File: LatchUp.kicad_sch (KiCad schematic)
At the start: 27 parts, among them Q10 IRF7406, Q11 BSL307SP, Q9 BSS138, U25 INA138NA_3K, U26 AD589JRZ, U27 LT1636CMS8_PBF

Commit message: Update the manufacturer part number for some of components to be compatible with avaiable parts in the JLC parts database
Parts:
- C101: JLCPCB Part # (none) -> C141069; Manufacturer_Part_Number (none) -> C0603C102K5RACAUTO
- C90, C91: JLCPCB Part # C1591 -> C129621; Manufacturer_Part_Number CL10B104KB8NNNC -> C0603C104K5RACAUTO
- C92: JLCPCB Part # C307479 -> C342956; Manufacturer_Part_Number CL10B105KA8NFNC -> CGA3E1X7R1V105KT000N
- D18: Manufacturer_Part_Number BZY55C2V7 RBG -> BZY55B2V7 RBG
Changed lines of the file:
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@@
       (effects (font (size 1.27 1.27)) hide)
     )
-    (property "JLCPCB Part #" "" (id 4) (at 88.9 91.44 0)
-      (effects (font (size 1.27 1.27)) hide)
-    )
-    (property "Manufacturer_Part_Number" "" (id 5) (at 88.9 91.44 0)
+    (property "JLCPCB Part #" "C141069" (id 4) (at 88.9 91.44 0)
+      (effects (font (size 1.27 1.27)) hide)
+    )
+    (property "Manufacturer_Part_Number" "C0603C102K5RACAUTO" (id 5) (at 88.9 91.44 0)
       (effects (font (size 1.27 1.27)) hide)
     )
@@
       (effects (font (size 1.27 1.27)) hide)
     )
-    (property "JLCPCB Part #" "C1591" (id 4) (at 30.48 81.28 0)
-      (effects (font (size 1.27 1.27)) hide)
-    )
-    (property "Manufacturer_Part_Number" "CL10B104KB8NNNC " (id 5) (at 30.48 81.28 0)
+    (property "JLCPCB Part #" "C129621" (id 4) (at 30.48 81.28 0)
+      (effects (font (size 1.27 1.27)) hide)
+    )
+    (property "Manufacturer_Part_Number" "C0603C104K5RACAUTO" (id 5) (at 30.48 81.28 0)
       (effects (font (size 1.27 1.27)) hide)
     )
@@
       (effects (font (size 1.27 1.27)) hide)
     )
-    (property "Manufacturer_Part_Number" "BZY55C2V7 RBG" (id 4) (at 180.34 100.33 90)
+    (property "Manufacturer_Part_Number" "BZY55B2V7 RBG " (id 4) (at 180.34 100.33 90)
       (effects (font (size 1.27 1.27)) hide)
     )
@@
       (effects (font (size 1.27 1.27)) hide)
     )
-    (property "JLCPCB Part #" "C1591" (id 4) (at 80.01 97.79 0)
-      (effects (font (size 1.27 1.27)) hide)
-    )
-    (property "Manufacturer_Part_Number" "CL10B104KB8NNNC " (id 5) (at 80.01 97.79 0)
+    (property "JLCPCB Part #" "C129621" (id 4) (at 80.01 97.79 0)
+      (effects (font (size 1.27 1.27)) hide)
+    )
+    (property "Manufacturer_Part_Number" "C0603C104K5RACAUTO" (id 5) (at 80.01 97.79 0)
       (effects (font (size 1.27 1.27)) hide)
     )
@@
       (effects (font (size 1.27 1.27)) hide)
     )
-    (property "JLCPCB Part #" "C307479" (id 4) (at 195.58 91.44 0)
-      (effects (font (size 1.27 1.27)) hide)
-    )
-    (property "Manufacturer_Part_Number" "CL10B105KA8NFNC " (id 5) (at 195.58 91.44 0)
-      (effects (font (size 1.27 1.27)) hide)
-    )
+    (property "JLCPCB Part #" "C342956" (id 4) (at 195.58 91.44 0)
+      (effects (font (size 1.27 1.27)) hide)
+    )
+    (property "Manufacturer_Part_Number" "CGA3E1X7R1V105KT000N" (id 5) (at 195.58 91.44 0)
+      (effects (font (size 1.27 1.27)) hide)
+    )

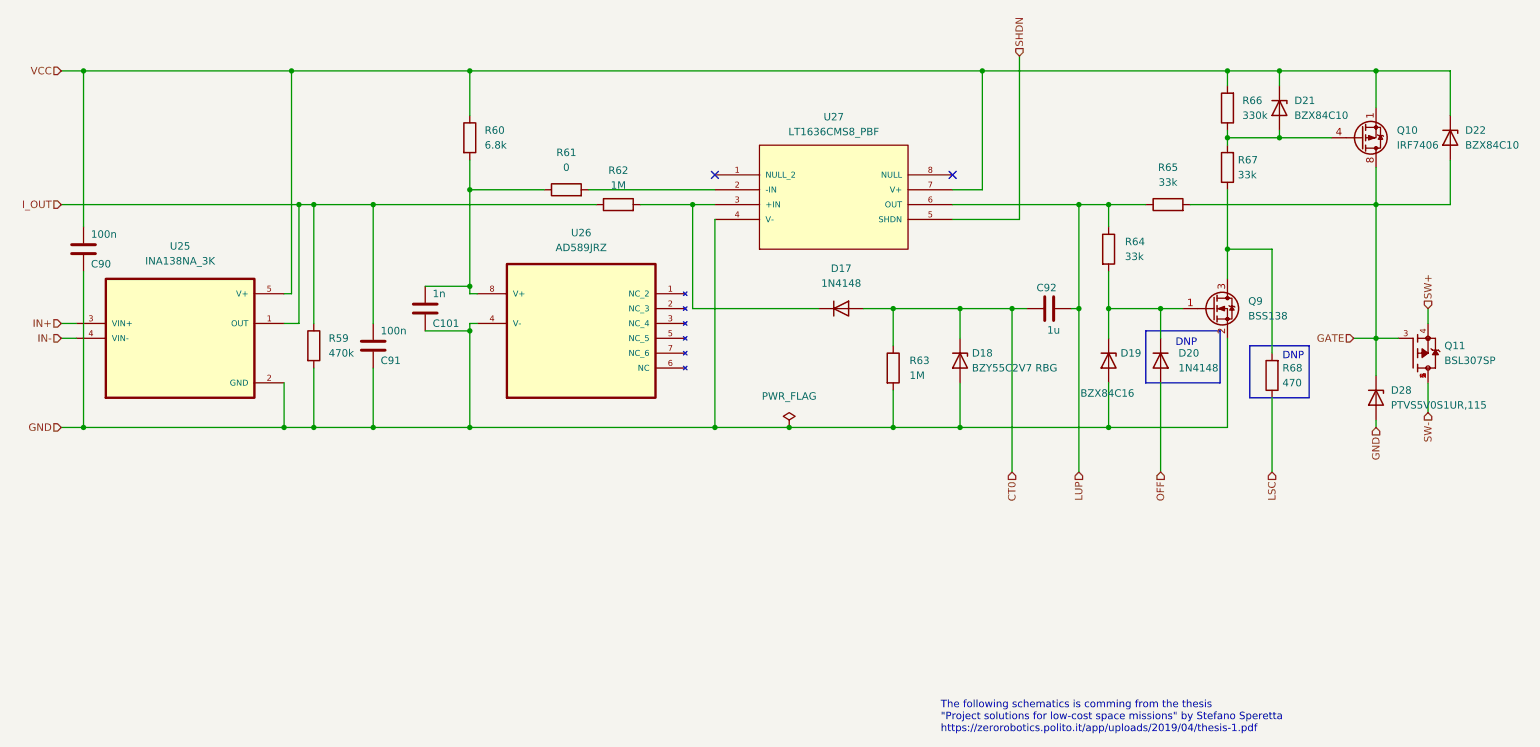
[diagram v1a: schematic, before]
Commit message: Update kicad files to v9.0 from v6.0
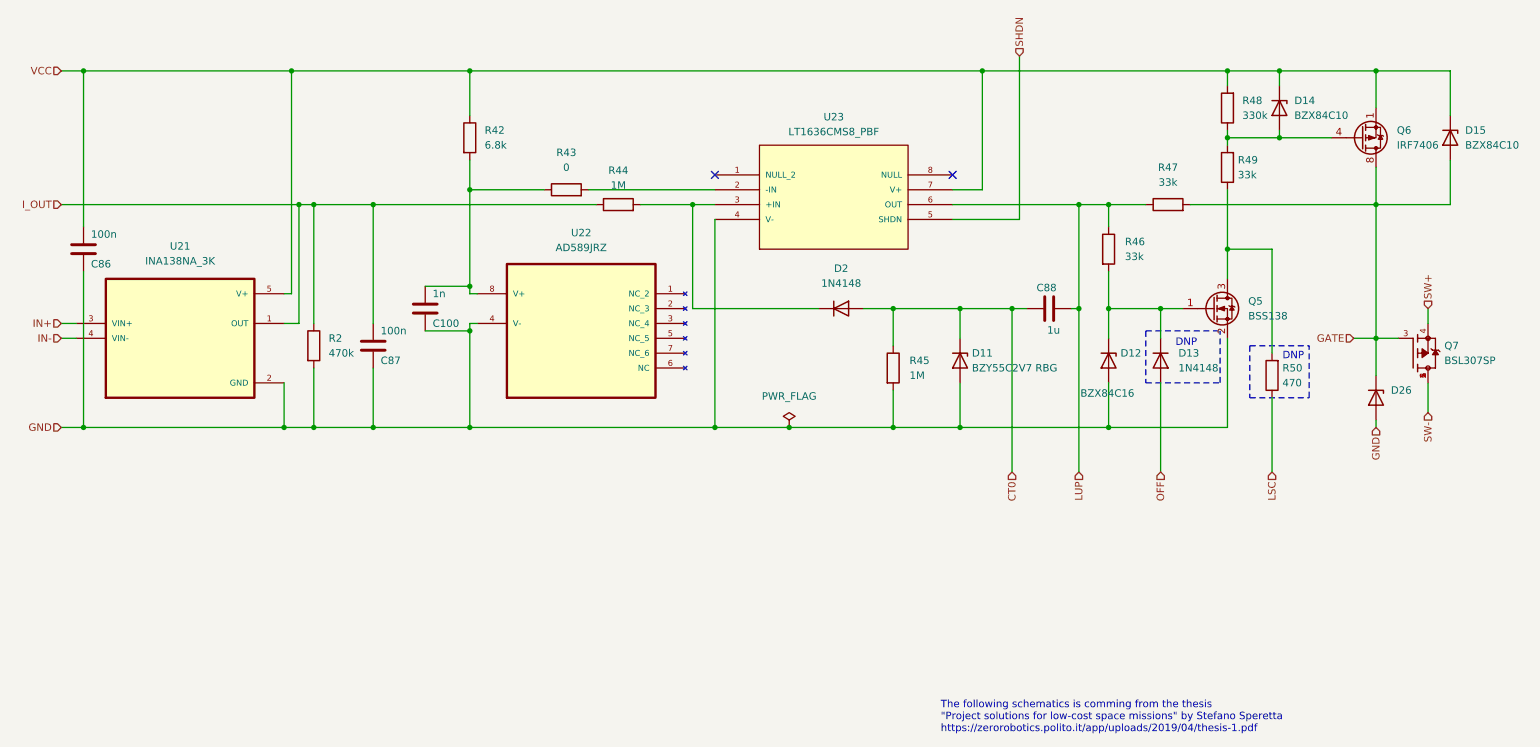
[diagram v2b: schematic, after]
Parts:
- D11: renamed from D18; value BZY55C2V7 RBG -> BZY55C2V7 RBG
- D26: renamed from D28; value PTVS5V0S1UR,115 -> PTVS5V0S1UR,115
- renumbered C101 to C100, C90 to C86, C91 to C87, C92 to C88, D19 to D12, D20 to D13, D21 to D14, D22 to D15, D17 to D2, Q9 to Q5, Q10 to Q6, Q11 to Q7, R59 to R2, R60 to R42, R61 to R43, R62 to R44, R63 to R45, R64 to R46, R65 to R47, R66 to R48, R67 to R49, R68 to R50, U25 to U21, U26 to U22, U27 to U23
